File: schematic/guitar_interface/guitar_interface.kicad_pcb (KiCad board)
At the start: 2 copper layers, 181 parts, among them IC1 LT1763IS8-5#TRPBF, IC2 LT1763CS8-3.3PBF, IC3 LTC1440IS8#TRPBF, IC4 PCM1808QPWRQ1, J1 Conn_ST_STDC14, J2 MUSBRM1C1M06, J3 Conn_01x02_Pin, J4 Conn_01x02_Pin, Q1 FDV301N, Q2 FDV304P, Q3 FDV304P, U1 LT3580xMS8E, U2 LT3580xMS8E, U3 LT1790-5, U4 LT1964-5, U5 OPA4134, U6 OPA4134, U8 STM32F446VETx, Y1 LFXTAL032878

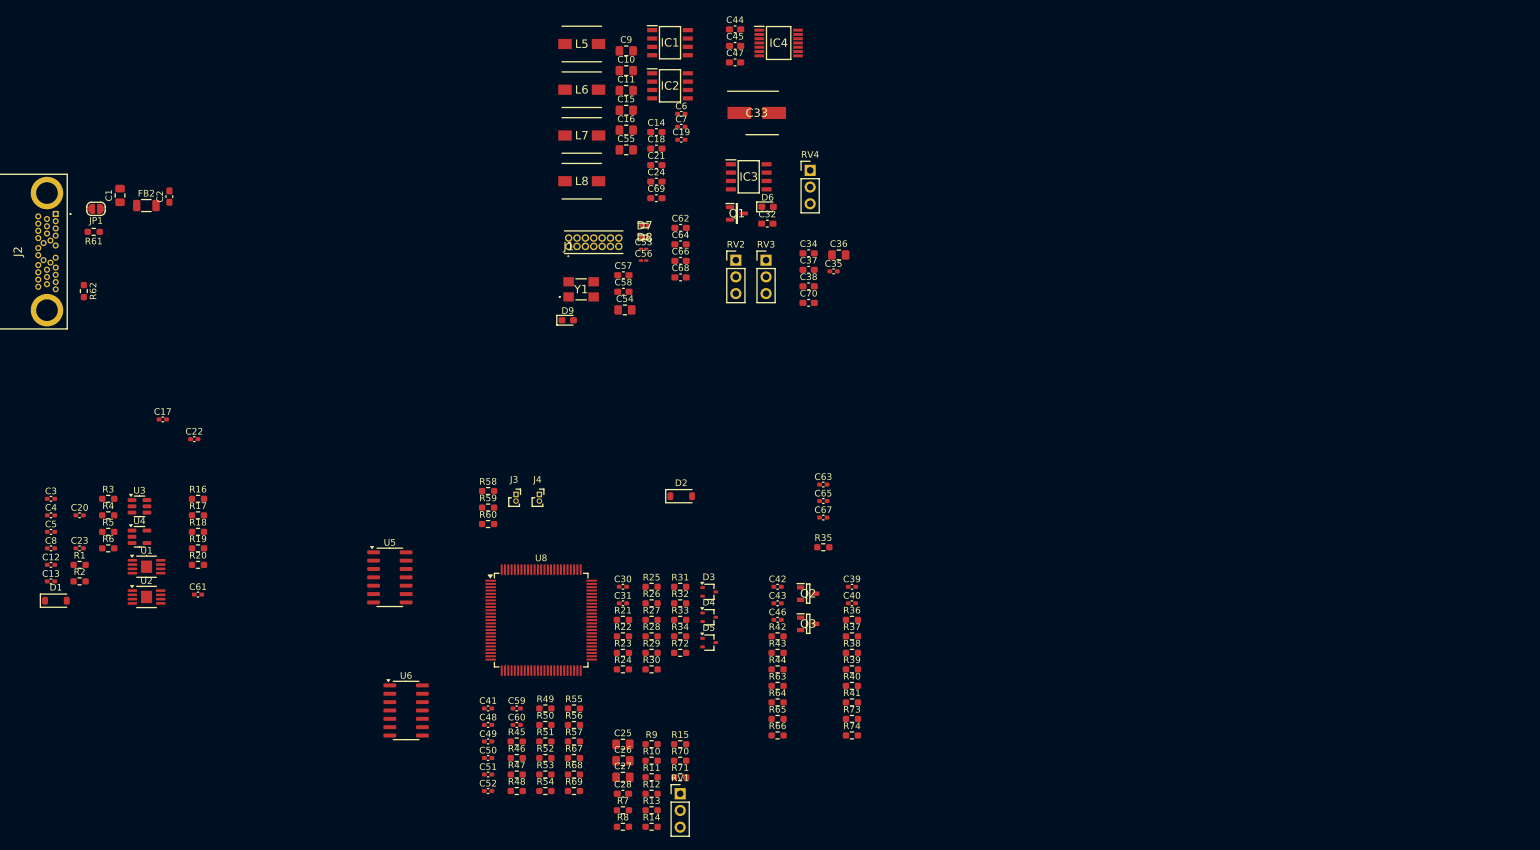
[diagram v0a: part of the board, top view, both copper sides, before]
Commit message: first scetch of audio pipeline and power supply layout
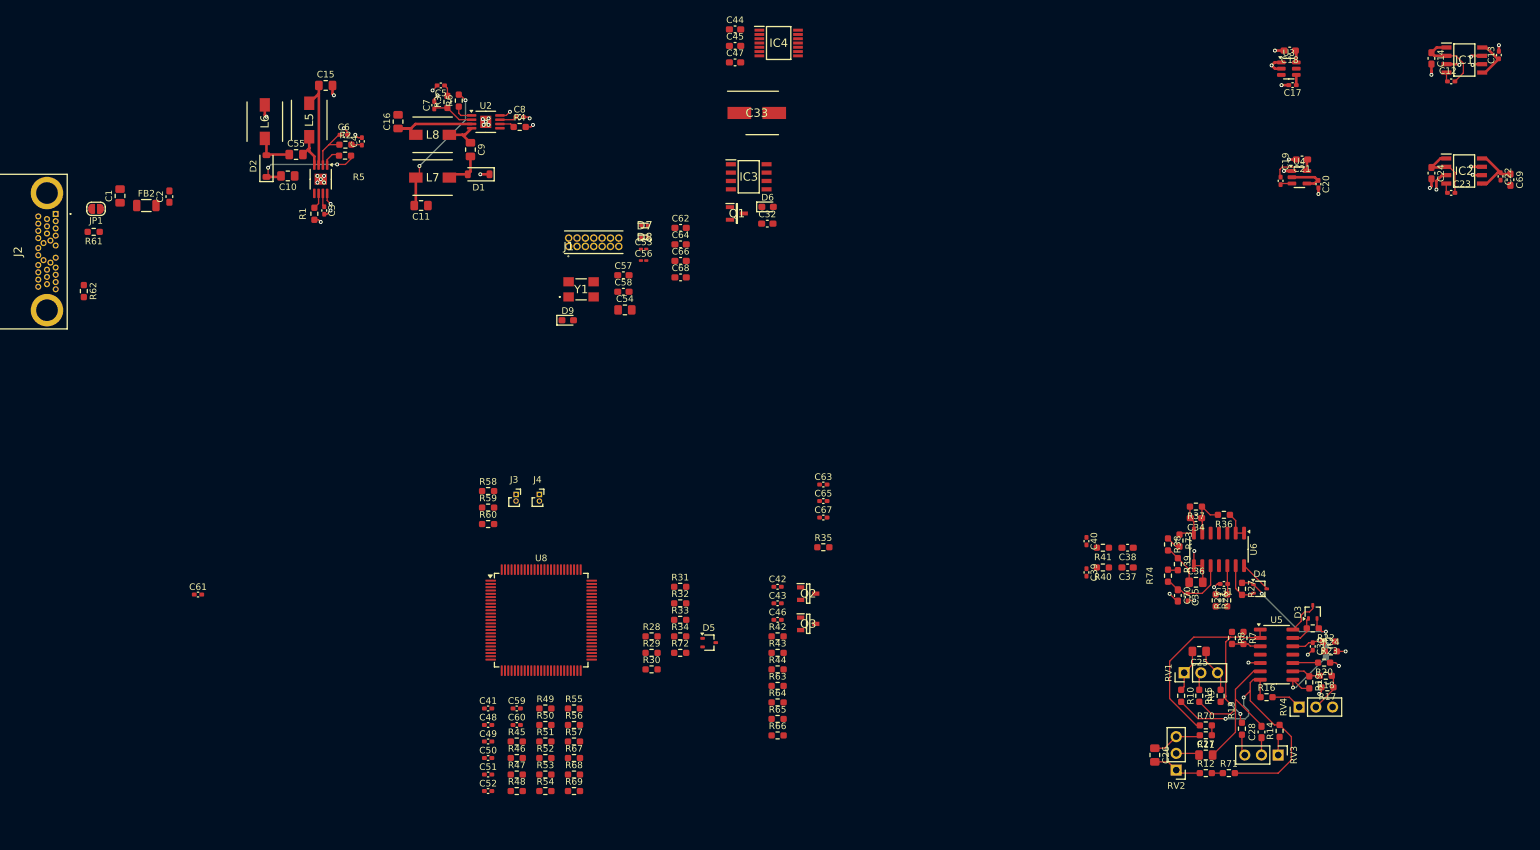
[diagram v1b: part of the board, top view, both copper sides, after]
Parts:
- R21: moved to B.Cu
- moved C13 234.1 mm to (263.0, 22.6), turned to 90 degrees
- moved C12 225.1 mm to (255.8, 26.6)
- moved C23 215.3 mm to (255.8, 43.6)
- moved C22 202.5 mm to (263.3, 41.1), turned to -90 degrees
- moved C20 194.9 mm to (235.6, 42.2), turned to -90 degrees
- moved U3 186.9 mm to (231.1, 24.7)
- moved U4 184.5 mm to (232.7, 41.2)
- moved C17 179.0 mm to (231.7, 27.2), turned to 180 degrees
- moved R17 173.6 mm to (237.0, 118.7), turned to 180 degrees
- moved R18 172.8 mm to (236.7, 117.0), turned to 180 degrees
- moved R20 171.8 mm to (236.5, 115.0), turned to 180 degrees
- moved R19 170.1 mm to (234.2, 118.0), turned to -90 degrees
- moved R16 165.1 mm to (227.7, 120.2)
- moved U5 135.3 mm to (229.2, 113.8)
- moved C69 129.8 mm to (264.8, 41.6), turned to -90 degrees
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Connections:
- C34 pad 1: Net-(U6C--) -> Net-(U6B--)
- C35 pad 1: Net-(U6B-+) -> Net-(U6C-+)
- C36 pad 2: Net-(U6B--) -> Net-(U6C--)
- C37 pad 1: Net-(U6B--) -> Net-(U6C--)
- C38 pad 1: Net-(U6B--) -> Net-(U6C--)
- C70 pad 1: Net-(U6B-+) -> Net-(U6C-+)
- R36 pad 2: Net-(U6C--) -> Net-(U6B--)
- R37 pad 1: Net-(U6C--) -> Net-(U6B--)
- R74 pad 2: Net-(U6B-+) -> Net-(U6C-+)
- U6 pad 10: GND -> Net-(U6C-+)
- U6 pad 5: Net-(U6B-+) -> GND
- U6 pad 7: Net-(U6B--) -> Net-(C34-Pad2)
- U6 pad 8: Net-(C34-Pad2) -> Net-(U6C--)
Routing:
- net GND: track 0.00 -> 58.1 mm, vias 0 -> 46
- net /Input and 3-band-eq/out: track 0.00 -> 44.6 mm, vias 0 -> 2
- net Net-(U5A--): track 0.00 -> 44.1 mm, vias 0 -> 2
- net /power_supply/5V: track 0.00 -> 38.9 mm
- net Net-(U5B--): track 0.00 -> 29.2 mm
- net /power_supply/-7V: track 0.00 -> 26.8 mm, vias 0 -> 2
- net /power_supply/7V: track 0.00 -> 25.6 mm, vias 0 -> 2
- net /adc preamp/in: track 0.00 -> 21.0 mm, vias 0 -> 2
- net /clipping stage/VDD_OPV: track 0.00 -> 11.4 mm
- net /clipping stage/in: track 0.00 -> 11.2 mm, vias 0 -> 1
- net Net-(U6C-+): track 0.00 -> 10.7 mm
- net /adc/VPP_3.3V: track 0.00 -> 9.87 mm
- net Net-(C26-Pad1): track 0.00 -> 7.65 mm
- net Net-(C26-Pad2): track 0.00 -> 7.55 mm
- net /clipping stage/VEE_OPV: track 0.00 -> 7.52 mm
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
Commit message: fix minor issues and do most of the pcb layout
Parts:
- C41, C48, C49, C50, C51, C54, C58, C59, C60, C61, C62, C63, C64, C65, C66, C67, C68: moved to B.Cu
- moved C61 184.1 mm to (247.4, 132.0), turned to -90 degrees
- moved J2 154.9 mm to (172.2, 133.4)
- moved JP1 154.9 mm to (178.3, 132.6)
- moved J3 154.3 mm to (256.5, 147.8)
- moved R61 154.1 mm to (176.8, 136.5)
- moved R62 153.4 mm to (176.0, 143.0)
- moved C1 149.8 mm to (178.5, 126.5), turned to 180 degrees
- moved C44 145.6 mm to (227.5, 140.0), turned to 180 degrees
- moved FB2 144.9 mm to (179.2, 124.0), turned to 180 degrees
- moved C16 144.1 mm to (209.2, 121.5), turned to 180 degrees
- moved D2 143.7 mm to (197.5, 115.8), turned to 180 degrees
- moved C11 142.6 mm to (222.0, 118.0), turned to -90 degrees
- moved C2 142.2 mm to (180.0, 122.0), turned to 180 degrees
- moved L6 142.2 mm to (190.8, 116.0), turned to 180 degrees
- moved C45 140.9 mm to (222.8, 140.0), turned to 180 degrees
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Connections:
- J1 pad 3: /mcu/3.3V -> /adc/VPP_3.3V
- R46 pad 2: /mcu/3.3V -> /adc/VPP_3.3V
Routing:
- net /adc/VPP_3.3V: track 9.87 -> 272.3 mm, vias 0 -> 15
- net GND: track 58.1 -> 165.9 mm, vias 46 -> 111
- net /power_supply/7V: track 25.6 -> 102.6 mm, vias 2 -> 5
- net /clipping stage/VEE_OPV: track 7.52 -> 78.9 mm, vias 0 -> 6
- net /power_supply/5V: track 38.9 -> 96.5 mm, vias 0 -> 2
- net /5V_USB: track 0.00 -> 51.4 mm, vias 0 -> 1
- net /adc/EN_VDD: track 0.00 -> 51.1 mm, vias 0 -> 3
- net /clipping stage/VDD_OPV: track 11.4 -> 55.1 mm, vias 0 -> 6
- net /Input and 3-band-eq/in: track 0.00 -> 29.1 mm, vias 0 -> 2
- net Net-(J2-SG1): track 0.00 -> 28.3 mm, vias 0 -> 1
- net /mcu/EN_PWR: track 0.00 -> 26.7 mm, vias 0 -> 2
- net Net-(J1-~{RST}): track 0.00 -> 25.1 mm, vias 0 -> 2
- net /adc preamp/in: track 21.0 -> 45.0 mm, vias 2 -> 5
- net /5V: track 0.00 -> 19.9 mm
- net Net-(U8-PE6): track 0.00 -> 19.4 mm
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- added copper zone on In1.Cu, net GND
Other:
- copper layers 2 -> 4

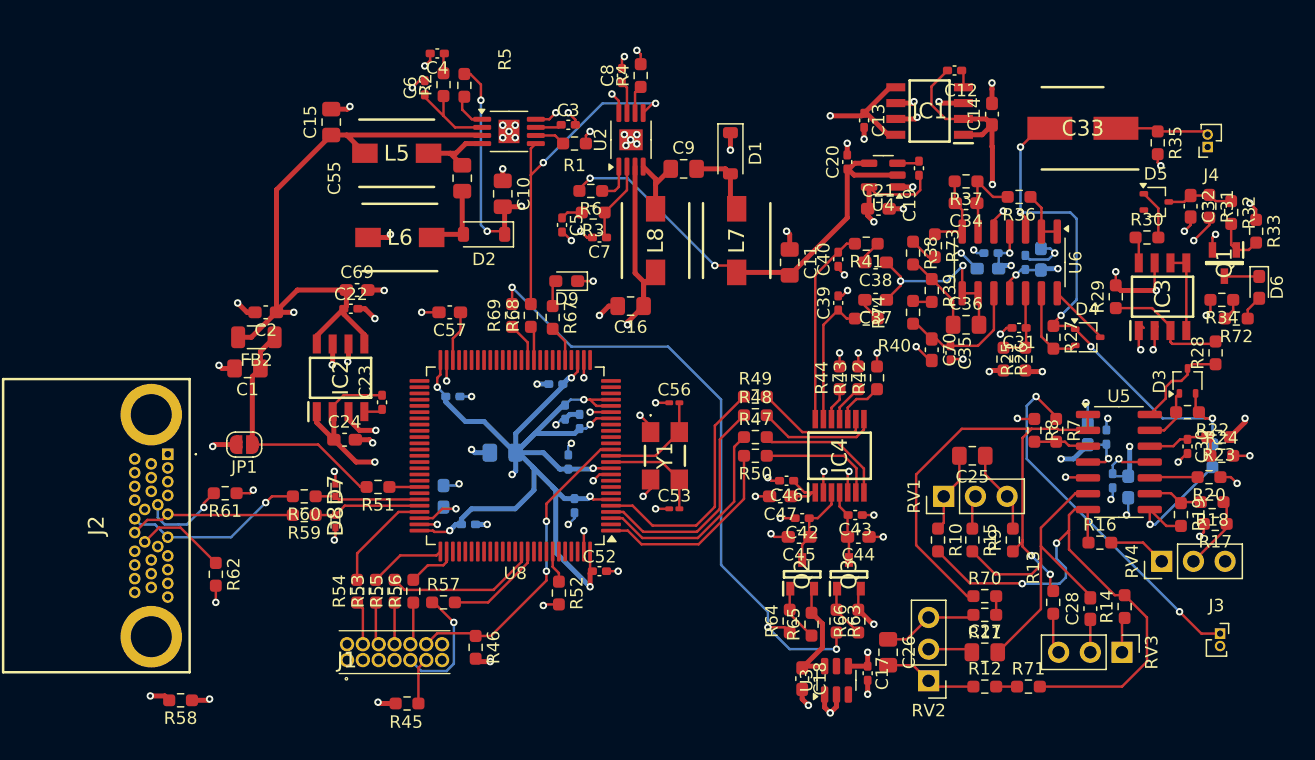
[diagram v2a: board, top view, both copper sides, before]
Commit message: refine layout fix, fix some minor issues, add additional ground planes on all layers, and add mounting holes
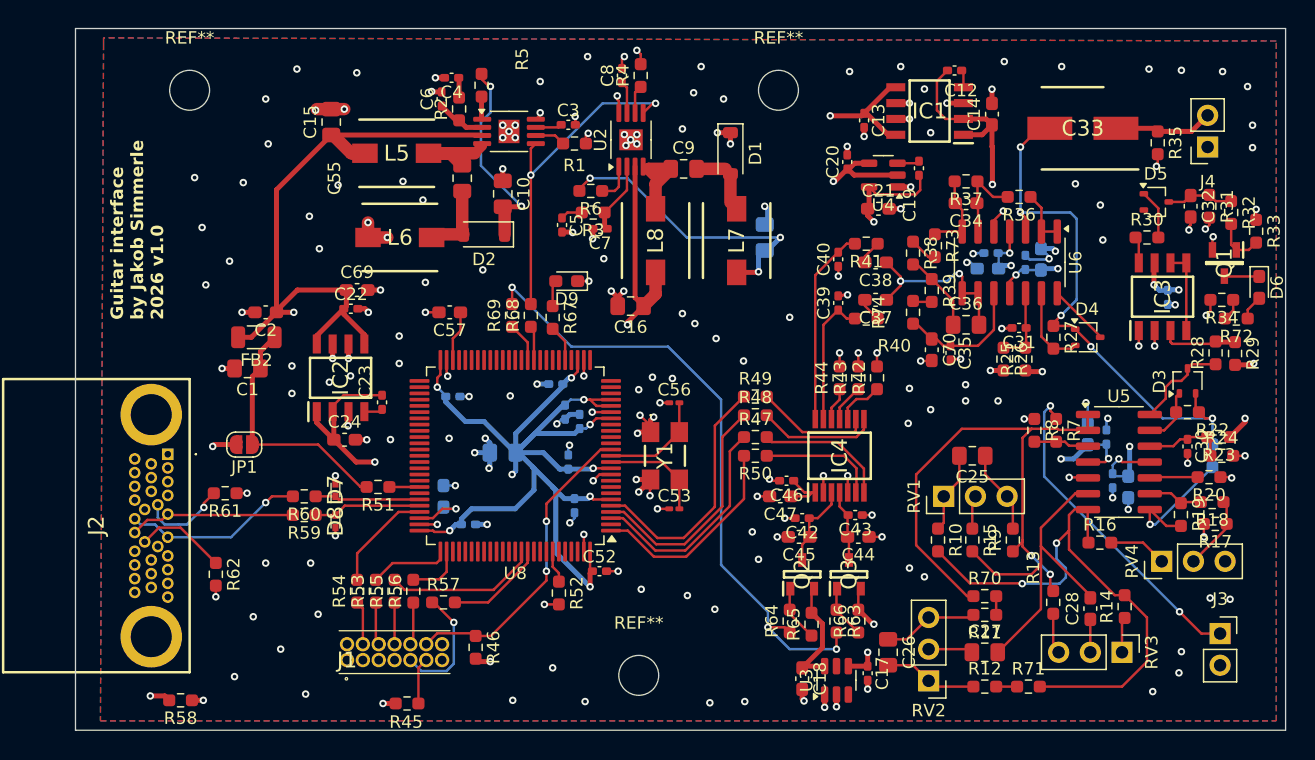
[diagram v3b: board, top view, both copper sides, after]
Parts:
- added C29: 100n, Capacitor_SMD:C_0402_1005Metric_Pad0.74x0.62mm_HandSolder, B.Cu at (252.3, 120.8)
- added REF**: MountingHole_3.2mm_M3, MountingHole:MountingHole_3.2mm_M3, F.Cu at (221.1, 104.2)
- added REF**: MountingHole_3.2mm_M3, MountingHole:MountingHole_3.2mm_M3, F.Cu at (209.9, 151.1)
- added REF**: MountingHole_3.2mm_M3, MountingHole:MountingHole_3.2mm_M3, F.Cu at (173.9, 104.2)
- C11: moved to B.Cu
- J3, J4: footprint Connector_PinSocket_1.00mm:PinSocket_1x02_P1.00mm_Vertical -> Connector_PinSocket_2.54mm:PinSocket_1x02_P2.54mm_Vertical
- moved R29 10.6 mm to (257.7, 125.3), turned to -90 degrees
- moved C11 2.83 mm to (220.0, 116.0)
- moved R2 2.32 mm to (195.5, 105.7)
- moved C4 2.26 mm to (194.9, 103.2)
- moved C6 1.62 mm to (194.1, 104.9)
- moved R5 1.38 mm to (197.3, 103.8)
- moved C7 0.70 mm to (206.8, 115.3)
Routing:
- net GND: track 165.9 -> 146.3 mm, vias 111 -> 209
- net /adc/VPP_3.3V: track 272.3 -> 264.3 mm, vias 15 -> 16
- net Net-(U1-VC): track 7.37 -> 3.96 mm
- net Net-(IC3-IN+): track 10.00 -> 6.58 mm
- net /Input and 3-band-eq/in: track 29.1 -> 26.4 mm
- net Net-(U1-SW): track 6.52 -> 9.05 mm
- net /power_supply/7V: track 102.6 -> 100.5 mm, vias 5 -> 4
- net Net-(U2-SW): track 5.51 -> 7.56 mm
- net /power_supply/-7V: track 37.2 -> 38.7 mm, vias 2 -> 4
- net Net-(U1-FB): track 3.10 -> 1.83 mm
- net Net-(U6C--): track 15.5 -> 14.4 mm
- net Net-(U8-PE4): track 17.2 -> 18.1 mm
- net Net-(U8-PE6): track 19.4 -> 20.2 mm
- net Net-(U8-PE2): track 16.1 -> 16.9 mm
- net Net-(U8-PE5): track 18.5 -> 19.3 mm
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- added copper zone on B.Cu, net GND
- added copper zone on F.Cu, net GND
- added copper zone on In2.Cu, net GND
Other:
- board outline added: 97 x 56.2 mm
- board text added: "Guitar interface by Jakob Simmerle 2026 v1.0"
